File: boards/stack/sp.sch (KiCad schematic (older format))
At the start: 24 parts, among them U3 SN74HC193PWR, U4 SN74HC193PWR, U5 74HC244, U6 74HC244

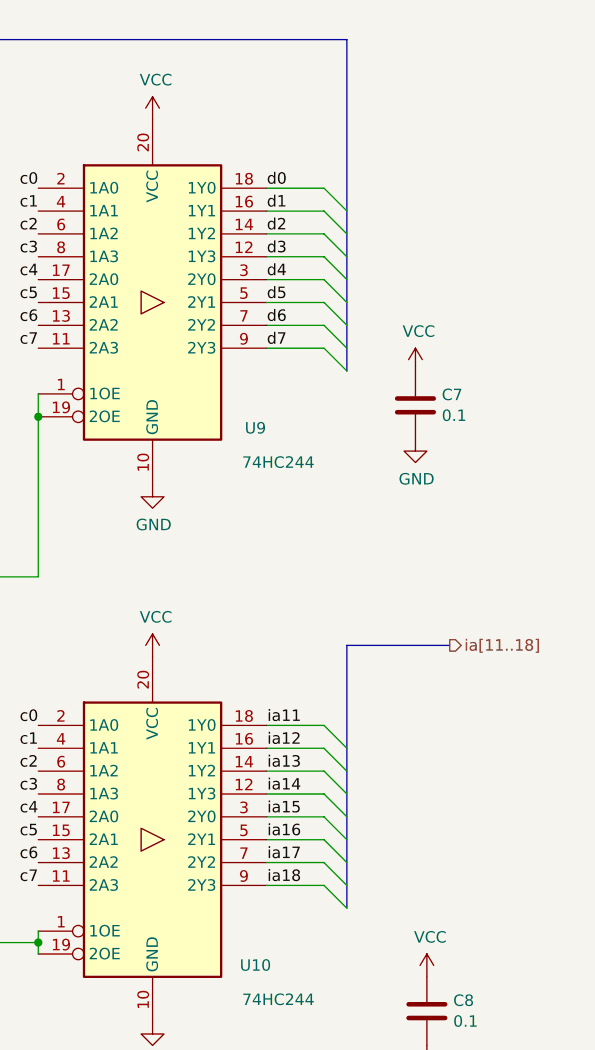
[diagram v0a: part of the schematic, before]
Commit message: Stack: values and footprints
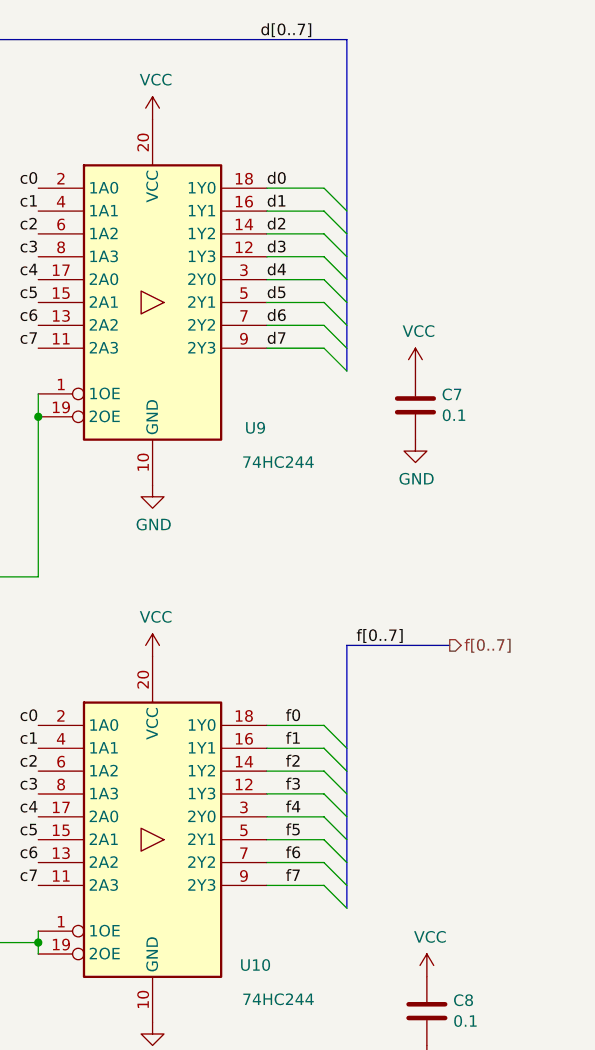
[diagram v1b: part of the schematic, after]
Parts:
- C1, C2, C3, C4: footprint (none) -> Capacitor_SMD:C_0805_2012Metric
- D1, D2, D3, D4, D5, D6, D7, D8: footprint (none) -> LED_SMD:LED_0805_2012Metric
- R1, R2, R3, R4, R5, R6, R7, R8: footprint (none) -> Resistor_SMD:R_0805_2012Metric
- U3, U4: footprint (none) -> Package_SO:TSSOP-16_4.4x5mm_P0.65mm
- U5, U6: footprint (none) -> Package_SO:TSSOP-20_4.4x6.5mm_P0.65mm
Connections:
- net ia11 renamed f0
- net ia12 renamed f1
- net ia13 renamed f2
- net ia14 renamed f3
- net ia15 renamed f4
- net ia16 renamed f5
- net ia17 renamed f6
- net ia18 renamed f7
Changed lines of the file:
@@
 F 0 "U7" H 5100 1250 50  0000 C CNN
 F 1 "SN74HC193PWR" H 5100 1100 50  0000 C CNN
-F 2 "" H 4600 1800 50  0001 C CNN
+F 2 "Package_SO:TSSOP-16_4.4x5mm_P0.65mm" H 4600 1800 50  0001 C CNN
 F 3 "http://www.ti.com/lit/ds/symlink/sn74ls193.pdf" H 4600 1800 50  0001 C CNN
 	1    4600 1800
@@
 F 0 "U8" H 5100 3750 50  0000 C CNN
 F 1 "SN74HC193PWR" H 5100 3600 50  0000 C CNN
-F 2 "" H 4600 4300 50  0001 C CNN
+F 2 "Package_SO:TSSOP-16_4.4x5mm_P0.65mm" H 4600 4300 50  0001 C CNN
 F 3 "http://www.ti.com/lit/ds/symlink/sn74ls193.pdf" H 4600 4300 50  0001 C CNN
 	1    4600 4300
@@
 F 0 "U9" H 8450 1300 50  0000 C CNN
 F 1 "74HC244" H 8550 1150 50  0000 C CNN
-F 2 "" H 8000 1850 50  0001 C CNN
+F 2 "Package_SO:TSSOP-20_4.4x6.5mm_P0.65mm" H 8000 1850 50  0001 C CNN
 F 3 "https://assets.nexperia.com/documents/data-sheet/74HC_HCT244.pdf" H 8000 1850 50  0001 C CNN
 	1    8000 1850
@@
 F 0 "U10" H 8450 3650 50  0000 C CNN
 F 1 "74HC244" H 8550 3500 50  0000 C CNN
-F 2 "" H 8000 4200 50  0001 C CNN
+F 2 "Package_SO:TSSOP-20_4.4x6.5mm_P0.65mm" H 8000 4200 50  0001 C CNN
 F 3 "https://assets.nexperia.com/documents/data-sheet/74HC_HCT244.pdf" H 8000 4200 50  0001 C CNN
 	1    8000 4200
@@
 $EndComp
 Text HLabel 9300 3350 2    50   Output ~ 0
-ia[11..18]
+f[0..7]
 Entry Wire Line
 	8750 3700 8850 3800
@@
 	8750 4400 8500 4400
 Text Label 8650 3700 2    50   ~ 0
-ia11
+f0
 Text Label 8650 3800 2    50   ~ 0
-ia12
+f1
 Text Label 8650 3900 2    50   ~ 0
-ia13
+f2
 Text Label 8650 4000 2    50   ~ 0
-ia14
+f3
 Text Label 8650 4100 2    50   ~ 0
-ia15
+f4
 Text Label 8650 4200 2    50   ~ 0
-ia16
+f5
 Text Label 8650 4300 2    50   ~ 0
-ia17
+f6
 Text Label 8650 4400 2    50   ~ 0
-ia18
+f7
 Wire Bus Line
 	8850 3350 9300 3350
@@
 F 0 "C5" H 6015 2346 50  0000 L CNN
 F 1 "0.1" H 6015 2255 50  0000 L CNN
-F 2 "" H 5938 2150 50  0001 C CNN
+F 2 "Capacitor_SMD:C_0805_2012Metric" H 5938 2150 50  0001 C CNN
 F 3 "~" H 5900 2300 50  0001 C CNN
 	1    5900 2300
@@
 F 0 "C7" H 9265 2346 50  0000 L CNN
 F 1 "0.1" H 9265 2255 50  0000 L CNN
-F 2 "" H 9188 2150 50  0001 C CNN
+F 2 "Capacitor_SMD:C_0805_2012Metric" H 9188 2150 50  0001 C CNN
 F 3 "~" H 9150 2300 50  0001 C CNN
 	1    9150 2300
@@
 F 0 "C6" H 6065 4996 50  0000 L CNN
 F 1 "0.1" H 6065 4905 50  0000 L CNN
-F 2 "" H 5988 4800 50  0001 C CNN
+F 2 "Capacitor_SMD:C_0805_2012Metric" H 5988 4800 50  0001 C CNN
 F 3 "~" H 5950 4950 50  0001 C CNN
 	1    5950 4950
@@
 F 0 "C8" H 9315 4996 50  0000 L CNN
 F 1 "0.1" H 9315 4905 50  0000 L CNN
-F 2 "" H 9238 4800 50  0001 C CNN
+F 2 "Capacitor_SMD:C_0805_2012Metric" H 9238 4800 50  0001 C CNN
 F 3 "~" H 9200 4950 50  0001 C CNN
 	1    9200 4950
@@
 F 0 "D9" H 4550 6000 50  0000 C CNN
 F 1 "LED" H 4550 6100 50  0000 C CNN
-F 2 "" H 5400 6100 50  0001 C CNN
+F 2 "LED_SMD:LED_0805_2012Metric" H 5400 6100 50  0001 C CNN
 F 3 "~" H 5400 6100 50  0001 C CNN
 	1    5400 6100
@@
 F 0 "R9" V 5600 6900 50  0000 C CNN
 F 1 "R" V 5700 6900 50  0000 C CNN
-F 2 "" V 5630 6100 50  0001 C CNN
+F 2 "Resistor_SMD:R_0805_2012Metric" V 5630 6100 50  0001 C CNN
 F 3 "~" H 5700 6100 50  0001 C CNN
 	1    5700 6100
@@
 F 0 "D10" H 4550 6200 50  0000 C CNN
 F 1 "LED" H 4550 6300 50  0000 C CNN
-F 2 "" H 5400 6300 50  0001 C CNN
+F 2 "LED_SMD:LED_0805_2012Metric" H 5400 6300 50  0001 C CNN
 F 3 "~" H 5400 6300 50  0001 C CNN
 	1    5400 6300
@@
 F 0 "R10" V 5600 7100 50  0000 C CNN
 F 1 "R" V 5700 7100 50  0000 C CNN
-F 2 "" V 5630 6300 50  0001 C CNN
+F 2 "Resistor_SMD:R_0805_2012Metric" V 5630 6300 50  0001 C CNN
 F 3 "~" H 5700 6300 50  0001 C CNN
 	1    5700 6300
@@
 F 0 "D11" H 4550 6400 50  0000 C CNN
 F 1 "LED" H 4550 6500 50  0000 C CNN
-F 2 "" H 5400 6500 50  0001 C CNN
+F 2 "LED_SMD:LED_0805_2012Metric" H 5400 6500 50  0001 C CNN
 F 3 "~" H 5400 6500 50  0001 C CNN
 	1    5400 6500
@@
 F 0 "R11" V 5600 7300 50  0000 C CNN
 F 1 "R" V 5700 7300 50  0000 C CNN
-F 2 "" V 5630 6500 50  0001 C CNN
+F 2 "Resistor_SMD:R_0805_2012Metric" V 5630 6500 50  0001 C CNN
 F 3 "~" H 5700 6500 50  0001 C CNN
 	1    5700 6500
@@
 F 0 "D12" H 4550 6600 50  0000 C CNN
 F 1 "LED" H 4550 6700 50  0000 C CNN
-F 2 "" H 5400 6700 50  0001 C CNN
+F 2 "LED_SMD:LED_0805_2012Metric" H 5400 6700 50  0001 C CNN
 F 3 "~" H 5400 6700 50  0001 C CNN
 	1    5400 6700
@@
 F 0 "R12" V 5600 7500 50  0000 C CNN
 F 1 "R" V 5700 7500 50  0000 C CNN
-F 2 "" V 5630 6700 50  0001 C CNN
+F 2 "Resistor_SMD:R_0805_2012Metric" V 5630 6700 50  0001 C CNN
 F 3 "~" H 5700 6700 50  0001 C CNN
 	1    5700 6700
@@
 F 0 "D13" H 4550 6800 50  0000 C CNN
 F 1 "LED" H 4550 6900 50  0000 C CNN
-F 2 "" H 5400 6900 50  0001 C CNN
+F 2 "LED_SMD:LED_0805_2012Metric" H 5400 6900 50  0001 C CNN
 F 3 "~" H 5400 6900 50  0001 C CNN
 	1    5400 6900
@@
 F 0 "R13" V 5600 7700 50  0000 C CNN
 F 1 "R" V 5700 7700 50  0000 C CNN
-F 2 "" V 5630 6900 50  0001 C CNN
+F 2 "Resistor_SMD:R_0805_2012Metric" V 5630 6900 50  0001 C CNN
 F 3 "~" H 5700 6900 50  0001 C CNN
 	1    5700 6900
@@
 F 0 "D14" H 4550 7000 50  0000 C CNN
 F 1 "LED" H 4550 7100 50  0000 C CNN
-F 2 "" H 5400 7100 50  0001 C CNN
+F 2 "LED_SMD:LED_0805_2012Metric" H 5400 7100 50  0001 C CNN
 F 3 "~" H 5400 7100 50  0001 C CNN
 	1    5400 7100
@@
 F 0 "R14" V 5600 7900 50  0000 C CNN
 F 1 "R" V 5700 7900 50  0000 C CNN
-F 2 "" V 5630 7100 50  0001 C CNN
+F 2 "Resistor_SMD:R_0805_2012Metric" V 5630 7100 50  0001 C CNN
 F 3 "~" H 5700 7100 50  0001 C CNN
 	1    5700 7100
@@
 F 0 "D15" H 4550 7200 50  0000 C CNN
 F 1 "LED" H 4550 7300 50  0000 C CNN
-F 2 "" H 5400 7300 50  0001 C CNN
+F 2 "LED_SMD:LED_0805_2012Metric" H 5400 7300 50  0001 C CNN
 F 3 "~" H 5400 7300 50  0001 C CNN
 	1    5400 7300
@@
 F 0 "R15" V 5600 8100 50  0000 C CNN
 F 1 "R" V 5700 8100 50  0000 C CNN
-F 2 "" V 5630 7300 50  0001 C CNN
+F 2 "Resistor_SMD:R_0805_2012Metric" V 5630 7300 50  0001 C CNN
 F 3 "~" H 5700 7300 50  0001 C CNN
 	1    5700 7300
@@
 F 0 "D16" H 4550 7400 50  0000 C CNN
 F 1 "LED" H 4550 7500 50  0000 C CNN
-F 2 "" H 5400 7500 50  0001 C CNN
+F 2 "LED_SMD:LED_0805_2012Metric" H 5400 7500 50  0001 C CNN
 F 3 "~" H 5400 7500 50  0001 C CNN
 	1    5400 7500
@@
 F 0 "R16" V 5600 8300 50  0000 C CNN
 F 1 "R" V 5700 8300 50  0000 C CNN
-F 2 "" V 5630 7500 50  0001 C CNN
+F 2 "Resistor_SMD:R_0805_2012Metric" V 5630 7500 50  0001 C CNN
 F 3 "~" H 5700 7500 50  0001 C CNN
 	1    5700 7500
@@
 Text Label 5250 7500 2    50   ~ 0
 c7
+Text Label 8700 700  2    50   ~ 0
+d[0..7]
+Text Label 9100 3350 2    50   ~ 0
+f[0..7]
 Wire Bus Line
 	3800 1200 3800 4100

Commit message: Stack: more values
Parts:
- D1, D2, D3, D4, D5, D6, D7, D8: value LED -> EAST2012RA1‎
- R1, R2, R3, R4, R5, R6, R7, R8: value R -> 160
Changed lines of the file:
@@
 $Descr A3 16535 11693
 encoding utf-8
-Sheet 2 3
+Sheet 3 3
 Title "Stack pointer"
 Date "2021-12-01"
@@
 AR Path="/61AB7A95/61B35202" Ref="D1"  Part="1"
 AR Path="/61AE3972/61B35202" Ref="D9"  Part="1"
-F 0 "D9" H 4550 6000 50  0000 C CNN
-F 1 "LED" H 4550 6100 50  0000 C CNN
+F 0 "D9" H 6050 6050 50  0000 C CNN
+F 1 "EAST2012RA1‎" H 6050 6150 50  0000 C CNN
 F 2 "LED_SMD:LED_0805_2012Metric" H 5400 6100 50  0001 C CNN
 F 3 "~" H 5400 6100 50  0001 C CNN
 	1    5400 6100
 	-1   0    0    1
-$EndComp
-$Comp
-L Device:R R1
-U 1 1 61B35FAA
-P 5700 6100
-AR Path="/61AB7A95/61B35FAA" Ref="R1"  Part="1"
-AR Path="/61AE3972/61B35FAA" Ref="R9"  Part="1"
-F 0 "R9" V 5600 6900 50  0000 C CNN
-F 1 "R" V 5700 6900 50  0000 C CNN
-F 2 "Resistor_SMD:R_0805_2012Metric" V 5630 6100 50  0001 C CNN
-F 3 "~" H 5700 6100 50  0001 C CNN
-	1    5700 6100
-	0    1    1    0
 $EndComp
 $Comp
@@
 AR Path="/61AB7A95/61B38641" Ref="D2"  Part="1"
 AR Path="/61AE3972/61B38641" Ref="D10"  Part="1"
-F 0 "D10" H 4550 6200 50  0000 C CNN
-F 1 "LED" H 4550 6300 50  0000 C CNN
+F 0 "D10" H 6050 6250 50  0000 C CNN
+F 1 "EAST2012RA1‎" H 6050 6350 50  0000 C CNN
 F 2 "LED_SMD:LED_0805_2012Metric" H 5400 6300 50  0001 C CNN
 F 3 "~" H 5400 6300 50  0001 C CNN
@@
 AR Path="/61AE3972/61B38647" Ref="R10"  Part="1"
 F 0 "R10" V 5600 7100 50  0000 C CNN
-F 1 "R" V 5700 7100 50  0000 C CNN
+F 1 "160" V 5700 7100 50  0000 C CNN
 F 2 "Resistor_SMD:R_0805_2012Metric" V 5630 6300 50  0001 C CNN
 F 3 "~" H 5700 6300 50  0001 C CNN
@@
 AR Path="/61AB7A95/61B3B16B" Ref="D3"  Part="1"
 AR Path="/61AE3972/61B3B16B" Ref="D11"  Part="1"
-F 0 "D11" H 4550 6400 50  0000 C CNN
-F 1 "LED" H 4550 6500 50  0000 C CNN
+F 0 "D11" H 6050 6450 50  0000 C CNN
+F 1 "EAST2012RA1‎" H 6050 6550 50  0000 C CNN
 F 2 "LED_SMD:LED_0805_2012Metric" H 5400 6500 50  0001 C CNN
 F 3 "~" H 5400 6500 50  0001 C CNN
@@
 AR Path="/61AE3972/61B3B171" Ref="R11"  Part="1"
 F 0 "R11" V 5600 7300 50  0000 C CNN
-F 1 "R" V 5700 7300 50  0000 C CNN
+F 1 "160" V 5700 7300 50  0000 C CNN
 F 2 "Resistor_SMD:R_0805_2012Metric" V 5630 6500 50  0001 C CNN
 F 3 "~" H 5700 6500 50  0001 C CNN
@@
 AR Path="/61AB7A95/61B3B17E" Ref="D4"  Part="1"
 AR Path="/61AE3972/61B3B17E" Ref="D12"  Part="1"
-F 0 "D12" H 4550 6600 50  0000 C CNN
-F 1 "LED" H 4550 6700 50  0000 C CNN
+F 0 "D12" H 6050 6650 50  0000 C CNN
+F 1 "EAST2012RA1‎" H 6050 6750 50  0000 C CNN
 F 2 "LED_SMD:LED_0805_2012Metric" H 5400 6700 50  0001 C CNN
 F 3 "~" H 5400 6700 50  0001 C CNN
@@
 AR Path="/61AE3972/61B3B184" Ref="R12"  Part="1"
 F 0 "R12" V 5600 7500 50  0000 C CNN
-F 1 "R" V 5700 7500 50  0000 C CNN
+F 1 "160" V 5700 7500 50  0000 C CNN
 F 2 "Resistor_SMD:R_0805_2012Metric" V 5630 6700 50  0001 C CNN
 F 3 "~" H 5700 6700 50  0001 C CNN
@@
 AR Path="/61AB7A95/61B411A6" Ref="D5"  Part="1"
 AR Path="/61AE3972/61B411A6" Ref="D13"  Part="1"
-F 0 "D13" H 4550 6800 50  0000 C CNN
-F 1 "LED" H 4550 6900 50  0000 C CNN
+F 0 "D13" H 6050 6850 50  0000 C CNN
+F 1 "EAST2012RA1‎" H 6050 6950 50  0000 C CNN
 F 2 "LED_SMD:LED_0805_2012Metric" H 5400 6900 50  0001 C CNN
 F 3 "~" H 5400 6900 50  0001 C CNN
@@
 AR Path="/61AE3972/61B411AC" Ref="R13"  Part="1"
 F 0 "R13" V 5600 7700 50  0000 C CNN
-F 1 "R" V 5700 7700 50  0000 C CNN
+F 1 "160" V 5700 7700 50  0000 C CNN
 F 2 "Resistor_SMD:R_0805_2012Metric" V 5630 6900 50  0001 C CNN
 F 3 "~" H 5700 6900 50  0001 C CNN
@@
 AR Path="/61AB7A95/61B411B9" Ref="D6"  Part="1"
 AR Path="/61AE3972/61B411B9" Ref="D14"  Part="1"
-F 0 "D14" H 4550 7000 50  0000 C CNN
-F 1 "LED" H 4550 7100 50  0000 C CNN
+F 0 "D14" H 6050 7050 50  0000 C CNN
+F 1 "EAST2012RA1‎" H 6050 7150 50  0000 C CNN
 F 2 "LED_SMD:LED_0805_2012Metric" H 5400 7100 50  0001 C CNN
 F 3 "~" H 5400 7100 50  0001 C CNN
@@
 AR Path="/61AE3972/61B411BF" Ref="R14"  Part="1"
 F 0 "R14" V 5600 7900 50  0000 C CNN
-F 1 "R" V 5700 7900 50  0000 C CNN
+F 1 "160" V 5700 7900 50  0000 C CNN
 F 2 "Resistor_SMD:R_0805_2012Metric" V 5630 7100 50  0001 C CNN
 F 3 "~" H 5700 7100 50  0001 C CNN
@@
 AR Path="/61AB7A95/61B411CC" Ref="D7"  Part="1"
 AR Path="/61AE3972/61B411CC" Ref="D15"  Part="1"
-F 0 "D15" H 4550 7200 50  0000 C CNN
-F 1 "LED" H 4550 7300 50  0000 C CNN
+F 0 "D15" H 6050 7250 50  0000 C CNN
+F 1 "EAST2012RA1‎" H 6050 7350 50  0000 C CNN
 F 2 "LED_SMD:LED_0805_2012Metric" H 5400 7300 50  0001 C CNN
 F 3 "~" H 5400 7300 50  0001 C CNN
@@
 AR Path="/61AE3972/61B411D2" Ref="R15"  Part="1"
 F 0 "R15" V 5600 8100 50  0000 C CNN
-F 1 "R" V 5700 8100 50  0000 C CNN
+F 1 "160" V 5700 8100 50  0000 C CNN
 F 2 "Resistor_SMD:R_0805_2012Metric" V 5630 7300 50  0001 C CNN
 F 3 "~" H 5700 7300 50  0001 C CNN
@@
 AR Path="/61AB7A95/61B411DF" Ref="D8"  Part="1"
 AR Path="/61AE3972/61B411DF" Ref="D16"  Part="1"
-F 0 "D16" H 4550 7400 50  0000 C CNN
-F 1 "LED" H 4550 7500 50  0000 C CNN
+F 0 "D16" H 6050 7450 50  0000 C CNN
+F 1 "EAST2012RA1‎" H 6050 7550 50  0000 C CNN
 F 2 "LED_SMD:LED_0805_2012Metric" H 5400 7500 50  0001 C CNN
 F 3 "~" H 5400 7500 50  0001 C CNN
@@
 AR Path="/61AE3972/61B411E5" Ref="R16"  Part="1"
 F 0 "R16" V 5600 8300 50  0000 C CNN
-F 1 "R" V 5700 8300 50  0000 C CNN
+F 1 "160" V 5700 8300 50  0000 C CNN
 F 2 "Resistor_SMD:R_0805_2012Metric" V 5630 7500 50  0001 C CNN
 F 3 "~" H 5700 7500 50  0001 C CNN
@@
 Wire Bus Line
 	8850 3350 8850 4500
+$Comp
+L Device:R R1
+U 1 1 61B35FAA
+P 5700 6100
+AR Path="/61AB7A95/61B35FAA" Ref="R1"  Part="1"
+AR Path="/61AE3972/61B35FAA" Ref="R9"  Part="1"
+F 0 "R9" V 5600 6900 50  0000 C CNN
+F 1 "160" V 5700 6900 50  0000 C CNN
+F 2 "Resistor_SMD:R_0805_2012Metric" V 5630 6100 50  0001 C CNN
+F 3 "~" H 5700 6100 50  0001 C CNN
+	1    5700 6100
+	0    1    1    0
+$EndComp
 $EndSCHEMATC

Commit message: Stack: board
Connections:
- net c0: now also U5.13 (2A2); no longer U5.2 (1A0)
- net c1: now also U5.11 (2A3); no longer U5.4 (1A1)
- net c6: now also U5.2 (1A0); no longer U5.13 (2A2)
- net c7: now also U5.4 (1A1); no longer U5.11 (2A3)
- net d0: now also U5.7 (2Y2); no longer U5.18 (1Y0)
- net d1: now also U5.9 (2Y3); no longer U5.16 (1Y1)
- net d6: now also U5.18 (1Y0); no longer U5.7 (2Y2)
- net d7: now also U5.16 (1Y1); no longer U5.9 (2Y3)
